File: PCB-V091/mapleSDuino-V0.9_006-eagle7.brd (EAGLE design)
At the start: 79 x 27 mm, 24 parts, among them IC2 LAN-USR-ES1

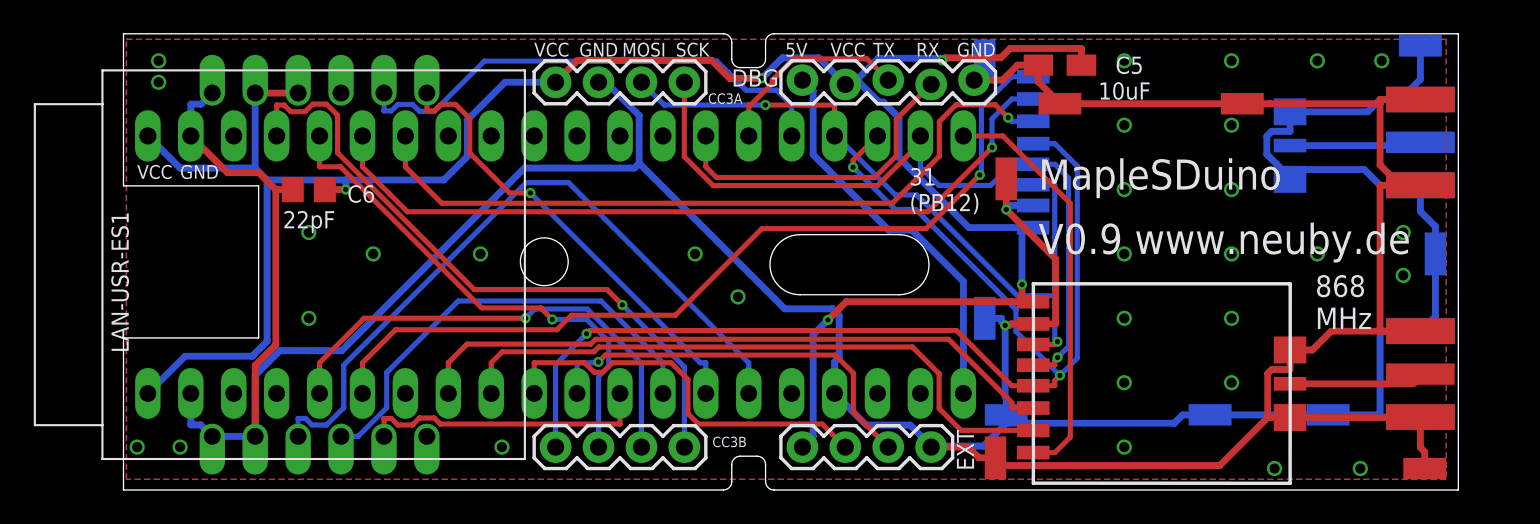
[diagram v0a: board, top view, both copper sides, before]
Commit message: Longer milling slot
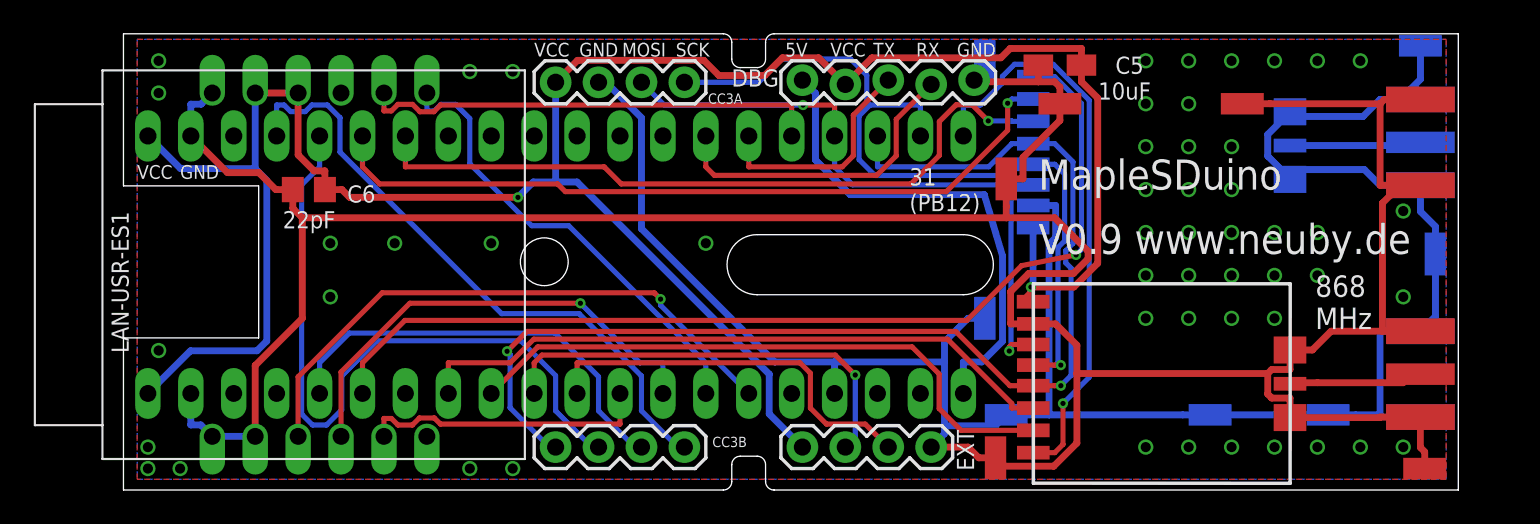
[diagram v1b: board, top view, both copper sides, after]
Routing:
- net GND: track 284.5 -> 316.0 mm, vias 33 -> 52
- net CC_IN_2: track 29.7 -> 41.8 mm, vias 1 -> 0
- net CC_CS0: track 24.4 -> 34.4 mm, vias 0 -> 1
- net CC_CS1: track 50.8 -> 59.1 mm
- net VCC: track 131.3 -> 139.3 mm, vias 5 -> 2
- net MOSI1: track 41.5 -> 34.9 mm, vias 0 -> 1
- net +5V: track 23.3 -> 29.4 mm
- net MISO2: track 73.9 -> 69.9 mm, vias 3 -> 2
- net MOSI2: track 42.9 -> 39.4 mm
- net SCK2: track 45.1 -> 48.1 mm
- net CC_OUT_2: track 28.5 -> 25.6 mm, vias 1 -> 0
- net WIZ_RST: track 29.7 -> 27.5 mm
- net TX2: track 23.9 -> 26.0 mm, vias 0 -> 1
- net TX1: track 11.8 -> 13.6 mm
- net CC_CS2: track 38.8 -> 37.1 mm, vias 1 -> 0
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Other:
- outline, holes or cut-outs redrawn
